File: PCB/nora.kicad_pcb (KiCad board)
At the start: 2 copper layers, 285 x 95.1 mm, 232 parts, among them J1 USB_C_Receptacle_USB2.0, J2 Conn_01x04, J3 Conn_01x02, J5 Conn_02x03_Odd_Even, U1 ATmega32U4-MU, U2 24LC64, U4 Pico, Y1 16MHz

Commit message: WIP 配線
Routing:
- net LED: track 49.1 -> 194.0 mm, vias 2 -> 4
- net PICO_VBUS: track 0.00 -> 103.8 mm, vias 0 -> 1
- net VCC: track 10.6 -> 26.7 mm, vias 0 -> 1
- net col0: track 284.3 -> 288.8 mm, vias 11 -> 13
- net Net-(D35-Pad2): track 0.00 -> 4.13 mm
- net +5V: track 124.3 -> 125.4 mm
- net col2: track 272.9 -> 272.3 mm

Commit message: WIP シルク重なり対応
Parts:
- moved EXT_R2 4.72 mm to (305.6, 67.6)
- moved EXT_C7 3.16 mm to (287.6, 106.7)
- moved EXT_R7 1.72 mm to (305.6, 73.3)
- moved EXT_C5 1.04 mm to (212.0, 111.8)
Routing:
- net SCL: track 41.7 -> 154.2 mm, vias 0 -> 2
- net SDA: track 39.1 -> 148.7 mm, vias 0 -> 2
- net +5V: track 125.4 -> 150.4 mm, vias 11 -> 12
- net GND: track 611.6 -> 633.9 mm, vias 2 -> 4
- net row9: track 397.0 -> 404.4 mm
- net LED_connection: track 76.7 -> 70.4 mm
- net col7: track 530.2 -> 525.9 mm, vias 10 -> 9
- net row2: track 305.1 -> 309.4 mm
- net row7: track 351.3 -> 354.8 mm
- net row6: track 310.9 -> 312.1 mm
- net RESET: track 85.5 -> 84.5 mm
- net col4: track 307.1 -> 308.0 mm
- net PICO_VBUS: track 103.8 -> 103.0 mm
- net col1: track 297.2 -> 297.8 mm
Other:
- board text added: "Bridge JP1 & JP2 to Pull-up(R4.7K) I2C"
- board text removed: "I2C Bridge JP1 & JP2 to Pull-up to R4.7K"

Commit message: WIP ロゴ配置調整中
H61.3ｍｍ
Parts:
- added G***: LOGO, locallib:Nora_logo_H61.3mm, B.Cu at (165.2, 64.8)
- moved U4 0.20 mm to (177.5, 36.5)
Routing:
- net LED: track 194.0 -> 176.3 mm
- net row6: track 312.1 -> 315.8 mm

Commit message: ロゴ配置
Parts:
- removed the G*** at (165.2, 64.8)
- added G***: LOGO, locallib:Nora_logo_H70.7mm, B.Cu at (171.1, 68.2)
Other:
- board text added: "for Outcast, Brave, Seeker, Adventurer, etc."
- board text removed: "for Outcast, Brave, Seeker, Adventurer, and so on"

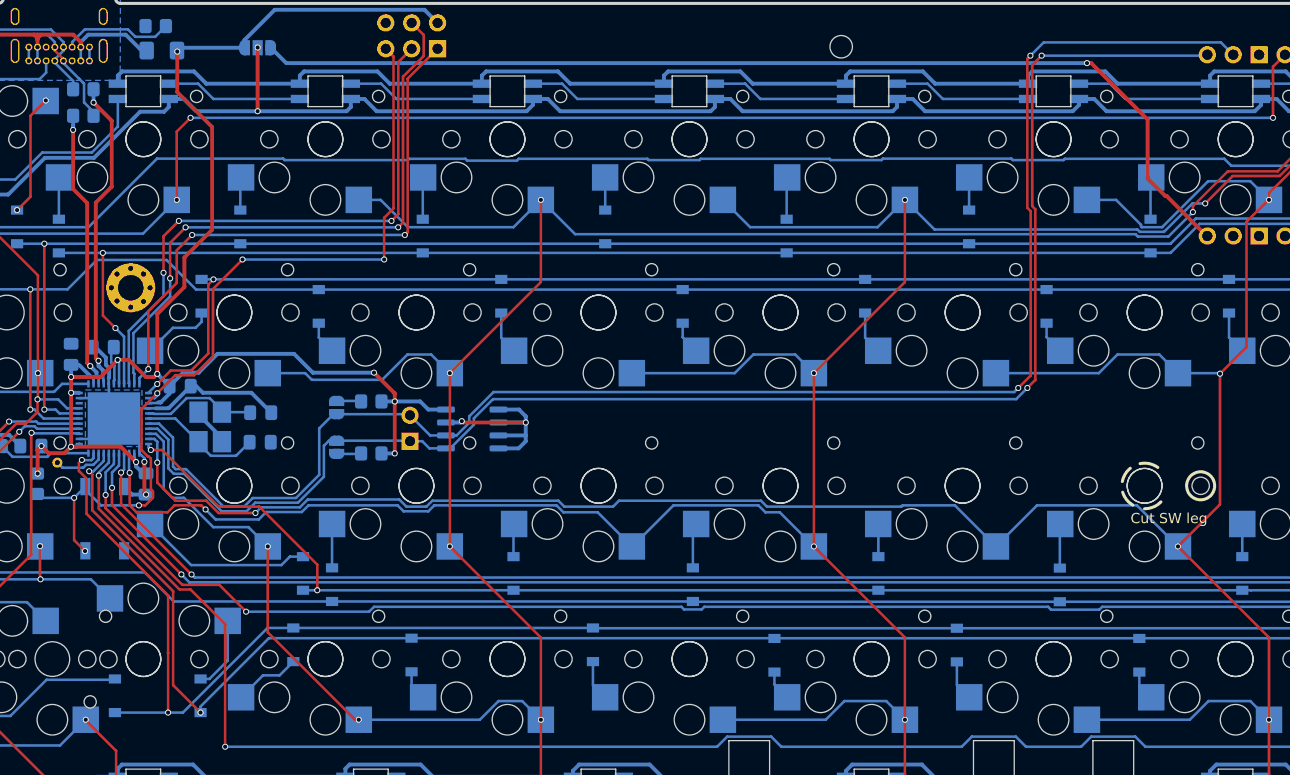
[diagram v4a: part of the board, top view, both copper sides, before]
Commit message: ロゴ配置完了, Renew logo on PCB #11
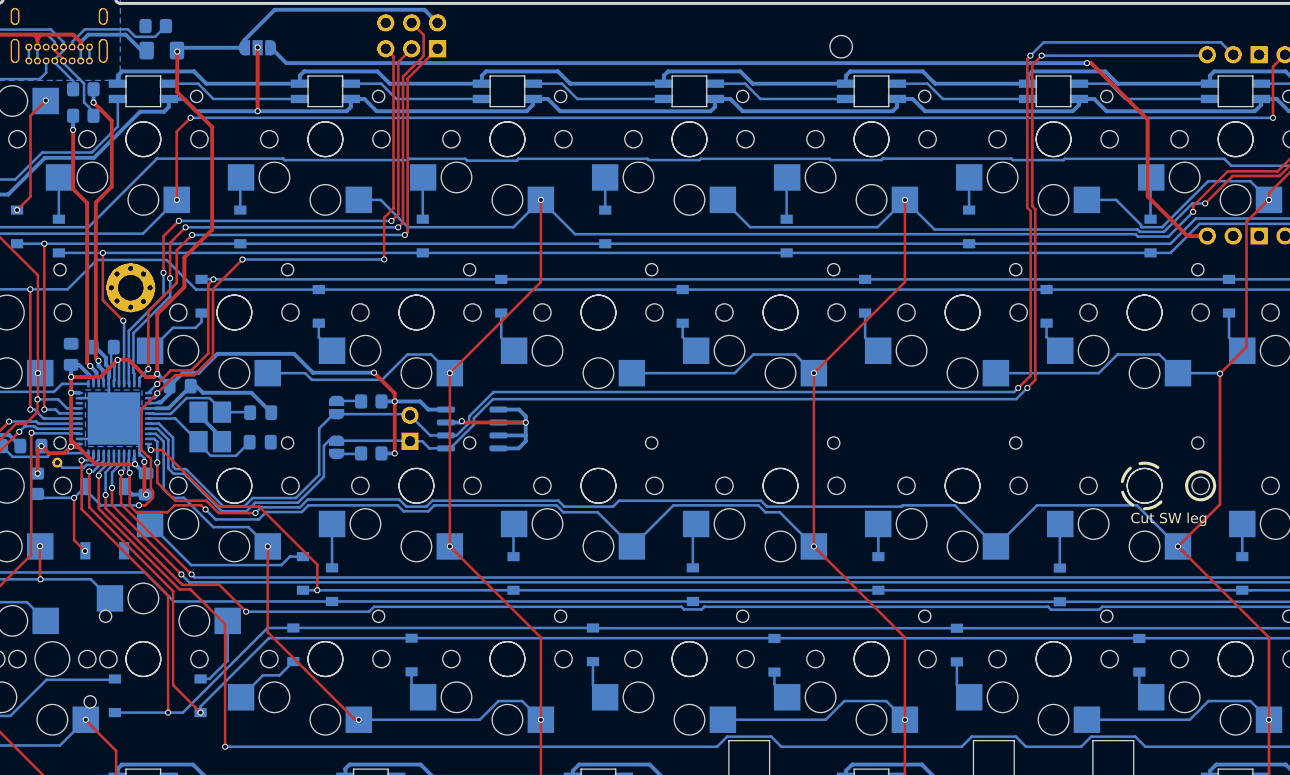
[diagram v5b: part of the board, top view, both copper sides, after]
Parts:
- D1, D11, D12, D13, D14, D15, D16, D17, D18, D19, D2, D20, D21, D22, D23, D25, D26, D27, D28, D29, D3, D30, D31, D32, D33, D35, D36, D37, D38, D39, D4, D40, D41, D42, D43, D45, D46, D47, D48, D49, D5, D50, D51, D52, D53, D54, D55, D56, D57, D58, D59, D6, D60, D61, D62, D63, D64, D65, D66, D67, D68, D69, D7, D70, D71, D72, D73, D74, D75, D76, D77, D78, D79, D8, D9: footprint locallib:D_SOD-123_Refelence@Left -> locallib:D_SOD-123-Pretty_No_Reference
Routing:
- net PICO_VBUS: track 102.9 -> 103.9 mm
- net +5V: track 150.4 -> 151.3 mm
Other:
- board text added: "Bridge JP1 & JP2 to Pull-up I2C"
- board text removed: "Bridge JP1 & JP2 to Pull-up(R4.7K) I2C"

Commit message: シルク位置調整#13
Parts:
- removed EXT_C6: Conn_01x01, TestPoint:TestPoint_THTPad_D1.5mm_Drill0.7mm
- added C6: Conn_01x01, TestPoint:TestPoint_THTPad_D1.5mm_Drill0.7mm, B.Cu at (270.9, 114.1)
- moved D10 0.37 mm to (31.7, 25.5), turned to 180 degrees
- moved J2 0.30 mm to (180.1, 24.7)
- renumbered EXT_C0 to C0, EXT_C1 to C1, EXT_C2 to C2, EXT_C3 to C3, EXT_C4 to C4, EXT_C5 to C5, EXT_C7 to C7, Ext_PC6 to PC6, EXT_R0 to R0, EXT_R1 to R1, EXT_R2 to R2, EXT_R3 to R3, EXT_R4 to R4, EXT_R5 to R5, EXT_R6 to R6, EXT_R7 to R7, EXT_R8 to R8, EXT_R9 to R9
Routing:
- net Net-(D10-Pad3): track 17.2 -> 19.6 mm
- net col4: track 308.2 -> 306.4 mm
- net Net-(D7-Pad2): track 7.31 -> 6.80 mm
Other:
- board text added: "Bridge to Pull-up I2C"
- board text added: "for Outcast, Brave, Seeker, Adventurer..."
- board text removed: "Bridge JP1 & JP2 to Pull-up I2C"
- board text removed: "for Outcast, Brave, Seeker, Adventurer, etc."
